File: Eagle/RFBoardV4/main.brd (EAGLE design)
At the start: 34.3 x 77.5 mm, 27 parts, among them Q1 8/16/20MHz, Q2 TIP41C, U1 ATMEGA328

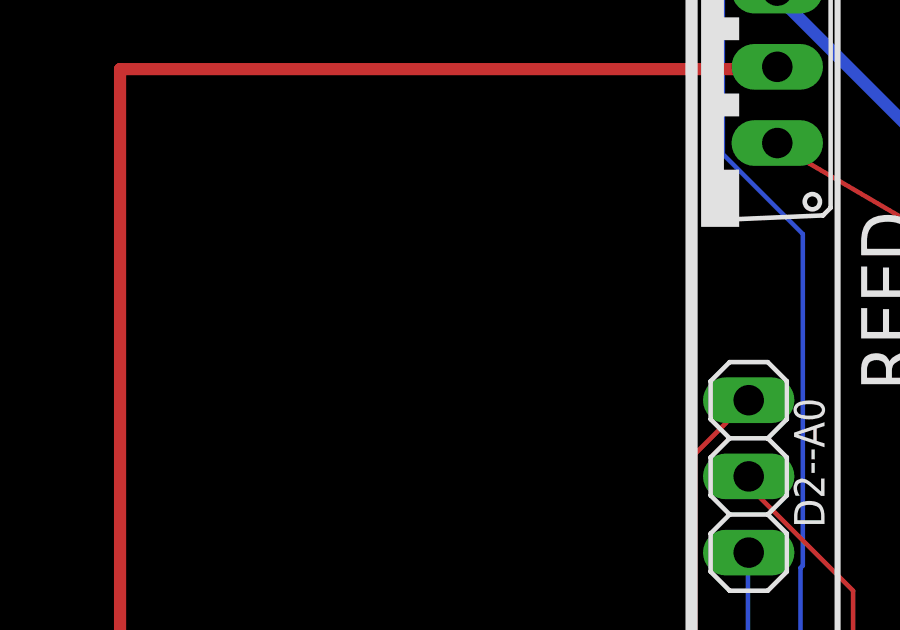
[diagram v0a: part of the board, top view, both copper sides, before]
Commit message: Added smaller mosfet - WIP
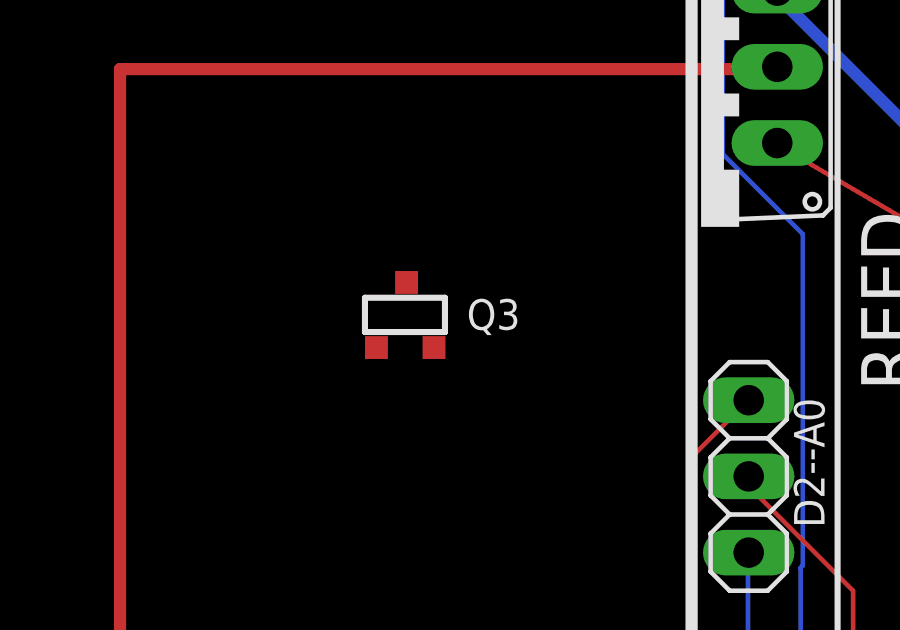
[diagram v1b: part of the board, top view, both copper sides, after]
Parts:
- added Q3: (no value), transistors:SOT-23
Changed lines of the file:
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@@
 </element>
 <element name="R4" library="SparkFun" package="0603-RES" value="10K" x="32.385" y="31.75" rot="R270"/>
+<element name="Q3" library="transistors" package="SOT-23" value="" x="15.875" y="62.5475"/>
 </elements>
 <signals>

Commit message: WIP
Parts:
- removed Q2: TIP41C, transistor-power:TO220AV
- added BATMIN1, BATPLUS1: (no value), pinhead:1X01
- moved Q3 15.5 mm to (27.6, 52.4), turned to 90 degrees
- moved D2--A0 13.7 mm to (27.3, 70.8)
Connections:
- removed net SCREW_PWR: JP4.2, Q2.E
- new net SCREW_GND: JP4.1, Q3.2
- net D5: now also Q3.1; no longer Q2.B
- net GND: now also BATMIN1.1, Q3.3; no longer JP4.1
- net VCC: now also BATPLUS1.1, JP4.2; no longer Q2.C
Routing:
- net REED_INT: track 80.3 -> 0.00 mm, vias 1 -> 0
- net VCC: track 152.3 -> 82.4 mm
- net D5: track 65.3 -> 0.00 mm, vias 2 -> 0
- net A0: track 48.6 -> 0.07 mm, vias 1 -> 0
- net REED/D3: track 42.4 -> 0.00 mm, vias 1 -> 0
- net SCREW_PWR: track 35.0 -> 0.00 mm
- net N$3: track 32.5 -> 0.00 mm
- net SCREW_TERM: track 13.8 -> 0.00 mm
- net GND: track 83.3 -> 75.5 mm, vias 8 -> 5

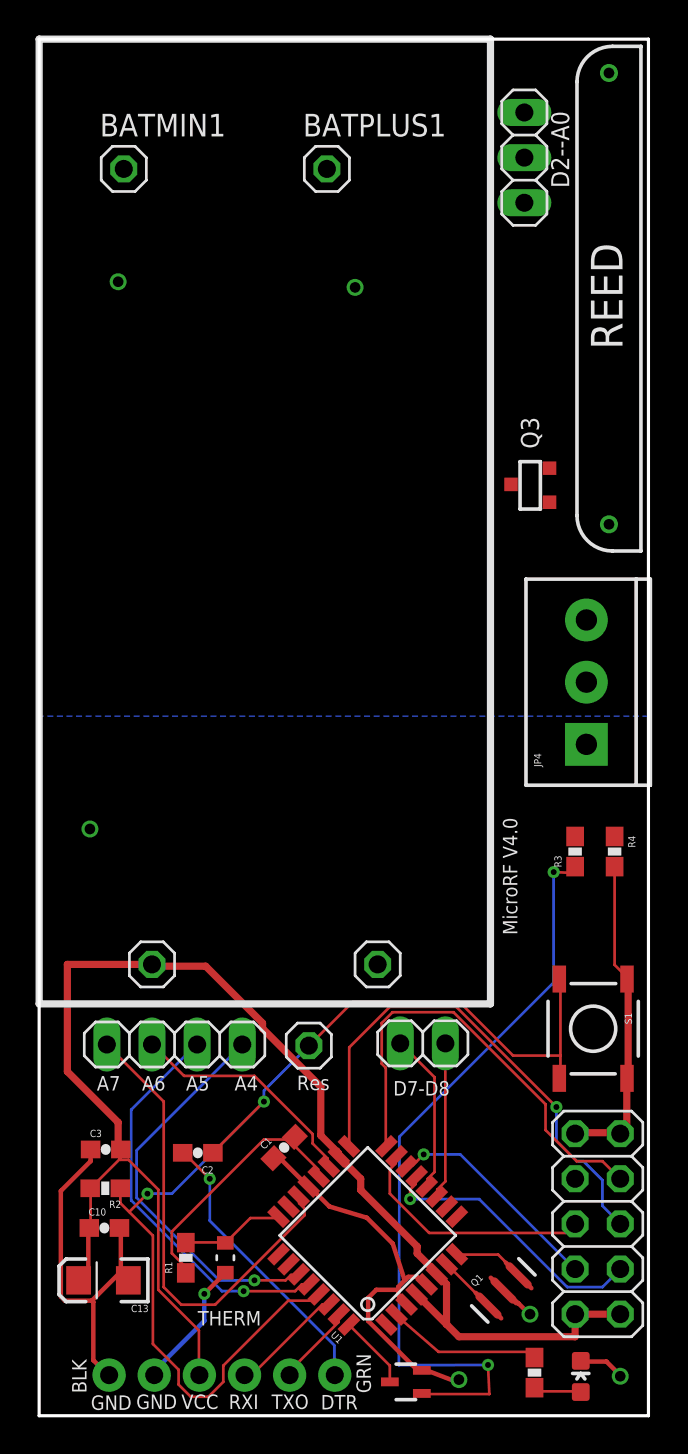
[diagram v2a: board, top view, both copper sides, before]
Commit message: V4
-Added mosfet to drive active sensors
-Added support for the X10 battery holders
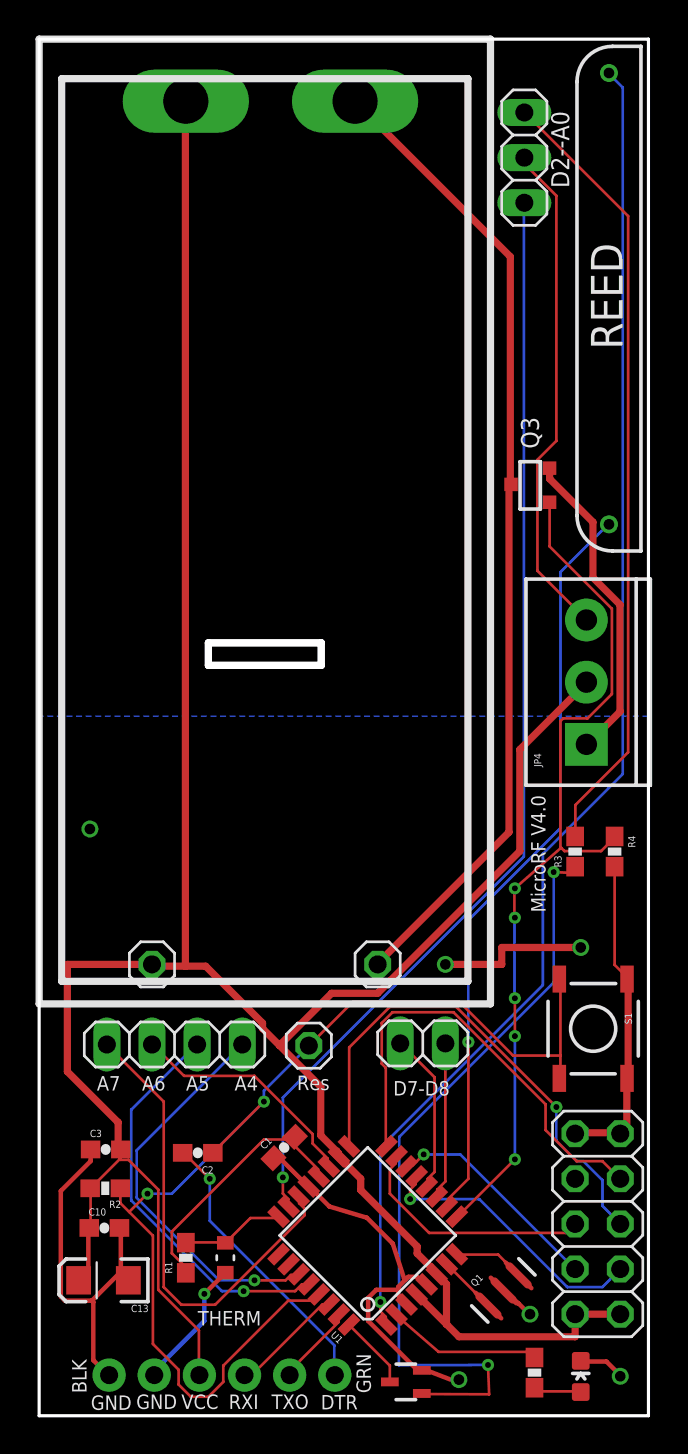
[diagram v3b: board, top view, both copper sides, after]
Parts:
- removed BATMIN1, BATPLUS1: (no value), pinhead:1X01
- added U$1: BAT, battery_wilkie:AAABATTERY
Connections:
- net GND: now also U$1.GND; no longer BATMIN1.1
- net VCC: now also U$1.VCC; no longer BATPLUS1.1
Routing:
- net VCC: track 82.4 -> 160.2 mm
- net REED_INT: track 0.00 -> 76.5 mm, vias 0 -> 1
- net GND: track 75.5 -> 139.4 mm, vias 5 -> 7
- net A0: track 0.07 -> 62.3 mm, vias 0 -> 1
- net D5: track 0.00 -> 49.7 mm, vias 0 -> 5
- net N$3: track 0.00 -> 44.4 mm
- net REED/D3: track 0.00 -> 42.2 mm, vias 0 -> 1
- net SCREW_TERM: track 0.00 -> 28.4 mm
- net SCREW_GND: track 0.00 -> 18.0 mm
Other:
- outline, holes or cut-outs redrawn

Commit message: Updated battery holes
- Added mill slots for battery
- Moved battery clip location

Still todo:
- Make holes smaller
- Move holes correct space apart
- Move clip rectangle to line up
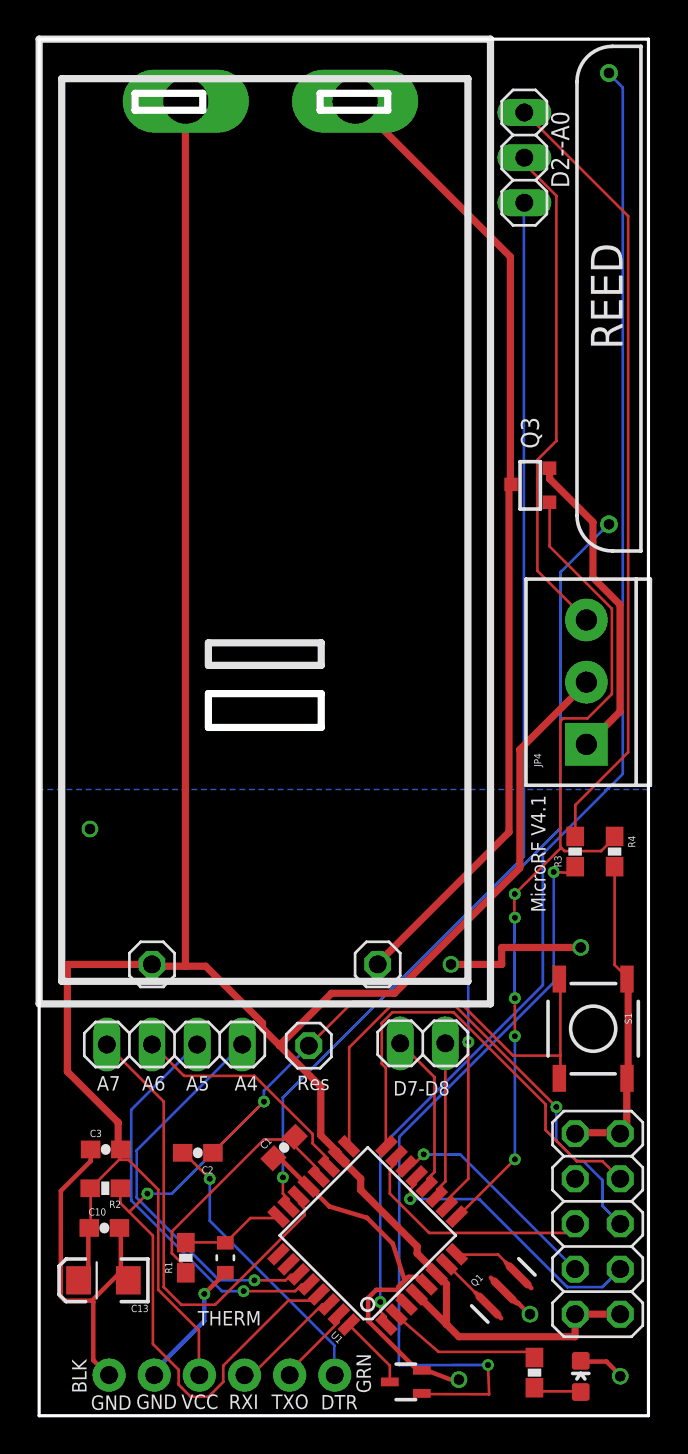
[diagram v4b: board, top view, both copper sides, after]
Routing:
- net VCC: track 160.2 -> 160.8 mm
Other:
- outline, holes or cut-outs redrawn
- board text added: "MicroRF V4.1"
- board text removed: "MicroRF V4.0"
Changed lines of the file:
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@@
 <text x="32.8295" y="60.0075" size="1.778" layer="21" rot="R90">REED</text>
 <text x="15.8496" y="0.3556" size="0.8128" layer="21" font="fixed" ratio="15">DTR</text>
-<text x="27.686" y="34.925" size="0.8128" layer="21" ratio="15" rot="R270">MicroRF V4.0</text>
+<text x="27.686" y="34.925" size="0.8128" layer="21" ratio="15" rot="R270">MicroRF V4.1</text>
 <text x="31.0515" y="4.7625" size="0.8128" layer="22" ratio="15" rot="MR90">VCC</text>
 <text x="31.877" y="17.018" size="0.8128" layer="22" ratio="15" rot="MR270">GND</text>
@@
 <text x="32.512" y="40.894" size="0.8128" layer="22" ratio="15" rot="MR0">3V (VCC)</text>
 <text x="32.512" y="37.4015" size="0.8128" layer="22" ratio="15" rot="MR0">GND</text>
-<wire x1="9.525" y1="43.4975" x2="9.525" y2="42.2275" width="0.4064" layer="20"/>
-<wire x1="9.525" y1="42.2275" x2="15.875" y2="42.2275" width="0.4064" layer="20"/>
-<wire x1="15.875" y1="42.2275" x2="15.875" y2="43.4975" width="0.4064" layer="20"/>
-<wire x1="15.875" y1="43.4975" x2="9.525" y2="43.4975" width="0.4064" layer="20"/>
+<wire x1="9.525" y1="40.64" x2="9.525" y2="38.735" width="0.4064" layer="20"/>
+<wire x1="9.525" y1="38.735" x2="15.875" y2="38.735" width="0.4064" layer="20"/>
+<wire x1="15.875" y1="38.735" x2="15.875" y2="40.64" width="0.4064" layer="20"/>
+<wire x1="15.875" y1="40.64" x2="9.525" y2="40.64" width="0.4064" layer="20"/>
+<wire x1="5.3975" y1="74.422" x2="5.3975" y2="73.4695" width="0.4064" layer="20"/>
+<wire x1="5.3975" y1="73.4695" x2="9.2075" y2="73.4695" width="0.4064" layer="20"/>
+<wire x1="9.2075" y1="73.4695" x2="9.2075" y2="74.422" width="0.4064" layer="20"/>
+<wire x1="9.2075" y1="74.422" x2="5.3975" y2="74.422" width="0.4064" layer="20"/>
+<wire x1="15.8115" y1="74.422" x2="15.8115" y2="73.4695" width="0.4064" layer="20"/>
+<wire x1="15.8115" y1="73.4695" x2="19.6215" y2="73.4695" width="0.4064" layer="20"/>
+<wire x1="19.6215" y1="73.4695" x2="19.6215" y2="74.422" width="0.4064" layer="20"/>
+<wire x1="19.6215" y1="74.422" x2="15.8115" y2="74.422" width="0.4064" layer="20"/>
 </plain>
 <attributes>
@@
 </class>
 </classes>
-<designrules name="LaenPCBOrder">
+<designrules name="OSHParkDRU">
 <description language="de">&lt;b&gt;EAGLE Design Rules&lt;/b&gt;
 &lt;p&gt;
@@
 <contactref element="Q1" pad="2"/>
 <polygon width="0.4064" layer="16">
-<vertex x="0" y="39.37"/>
+<vertex x="0" y="35.2425"/>
 <vertex x="0" y="0"/>
 <vertex x="34.29" y="0"/>
-<vertex x="34.29" y="39.37"/>
+<vertex x="34.29" y="35.2425"/>
 </polygon>
 <via x="27.6225" y="5.715" extent="1-16" drill="0.6"/>
@@
 <wire x1="26.4414" y1="52.2732" x2="26.5557" y2="52.4129" width="0.4064" layer="1"/>
 <wire x1="19.05" y1="25.4508" x2="19.05" y2="25.4" width="0.4064" layer="1"/>
-<via x="22.86" y="25.4" extent="1-16" drill="0.6"/>
+<via x="23.1775" y="25.4" extent="1-16" drill="0.6"/>
 <via x="30.48" y="26.3525" extent="1-16" drill="0.6"/>
-<wire x1="22.86" y1="25.4" x2="26.035" y2="25.4" width="0.4064" layer="1"/>
+<wire x1="23.1775" y1="25.4" x2="26.035" y2="25.4" width="0.4064" layer="1"/>
 <wire x1="26.035" y1="25.4" x2="26.035" y2="26.3525" width="0.4064" layer="1"/>
 <wire x1="26.035" y1="26.3525" x2="30.48" y2="26.3525" width="0.4064" layer="1"/>
@@
 <contactref element="U$1" pad="VCC"/>
 <wire x1="27.051" y1="37.4904" x2="30.7848" y2="41.2242" width="0.4064" layer="1"/>
-<wire x1="27.051" y1="31.7754" x2="27.051" y2="37.4904" width="0.4064" layer="1"/>
-<wire x1="19.05" y1="23.7744" x2="27.051" y2="31.7754" width="0.4064" layer="1"/>
-<wire x1="16.4592" y1="23.7744" x2="19.05" y2="23.7744" width="0.4064" layer="1"/>
+<wire x1="27.051" y1="30.8229" x2="27.051" y2="37.4904" width="0.4064" layer="1"/>
+<wire x1="20.0025" y1="23.7744" x2="27.051" y2="30.8229" width="0.4064" layer="1"/>
+<wire x1="16.4592" y1="23.7744" x2="20.0025" y2="23.7744" width="0.4064" layer="1"/>
 <wire x1="13.5255" y1="20.8407" x2="16.4592" y2="23.7744" width="0.4064" layer="1"/>
 <wire x1="30.7848" y1="41.2242" x2="30.7975" y2="41.2825" width="0.4064" layer="1"/>
@@
 <wire x1="26.7716" y1="14.4272" x2="23.5458" y2="11.2014" width="0.1524" layer="1"/>
 <wire x1="26.7716" y1="21.3614" x2="26.7716" y2="14.4272" width="0.1524" layer="16"/>
-<wire x1="29.3751" y1="31.9659" x2="26.7716" y2="29.6799" width="0.1524" layer="1"/>
+<wire x1="29.3751" y1="31.9659" x2="26.7716" y2="29.3624" width="0.1524" layer="1"/>
 <wire x1="23.5458" y1="11.2014" x2="23.505940625" y2="11.2013375" width="0.1524" layer="1"/>
 <via x="26.7716" y="14.4272" extent="1-16" drill="0.3302"/>
 <via x="26.7716" y="21.3614" extent="1-16" drill="0.3302"/>
 <via x="26.7716" y="28.0289" extent="1-16" drill="0.3302"/>
-<via x="26.7716" y="29.6799" extent="1-16" drill="0.3302"/>
+<via x="26.7716" y="29.3624" extent="1-16" drill="0.3302"/>
 <via x="26.7716" y="23.495" extent="1-16" drill="0.3302"/>
 <wire x1="26.7716" y1="23.495" x2="26.7716" y2="21.3614" width="0.1524" layer="1"/>
 <wire x1="26.7462" y1="29.6418" x2="26.7462" y2="28.0416" width="0.1524" layer="1"/>
 <wire x1="26.7462" y1="28.0416" x2="26.7716" y2="28.0289" width="0.1524" layer="1"/>
-<wire x1="26.7462" y1="29.6418" x2="26.7716" y2="29.6799" width="0.1524" layer="1"/>
+<wire x1="26.7462" y1="29.6418" x2="26.7716" y2="29.3624" width="0.1524" layer="1"/>
 <wire x1="26.7462" y1="23.5458" x2="26.7462" y2="27.9654" width="0.1524" layer="16"/>
 <wire x1="26.7462" y1="27.9654" x2="26.7716" y2="28.0289" width="0.1524" layer="16"/>
